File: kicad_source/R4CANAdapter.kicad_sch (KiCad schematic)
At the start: 32 parts, among them CN1 CONN_01X05, CN2 691322310004, CN3 GH_SM04B-GHS-TB, CN4 GH_SM04B-GHS-TB, CN5 SM04B-SRSS-TB, Q1 2N7002, Q2 2N7002, U1 MCP2551-I/SN, U2 24LC64

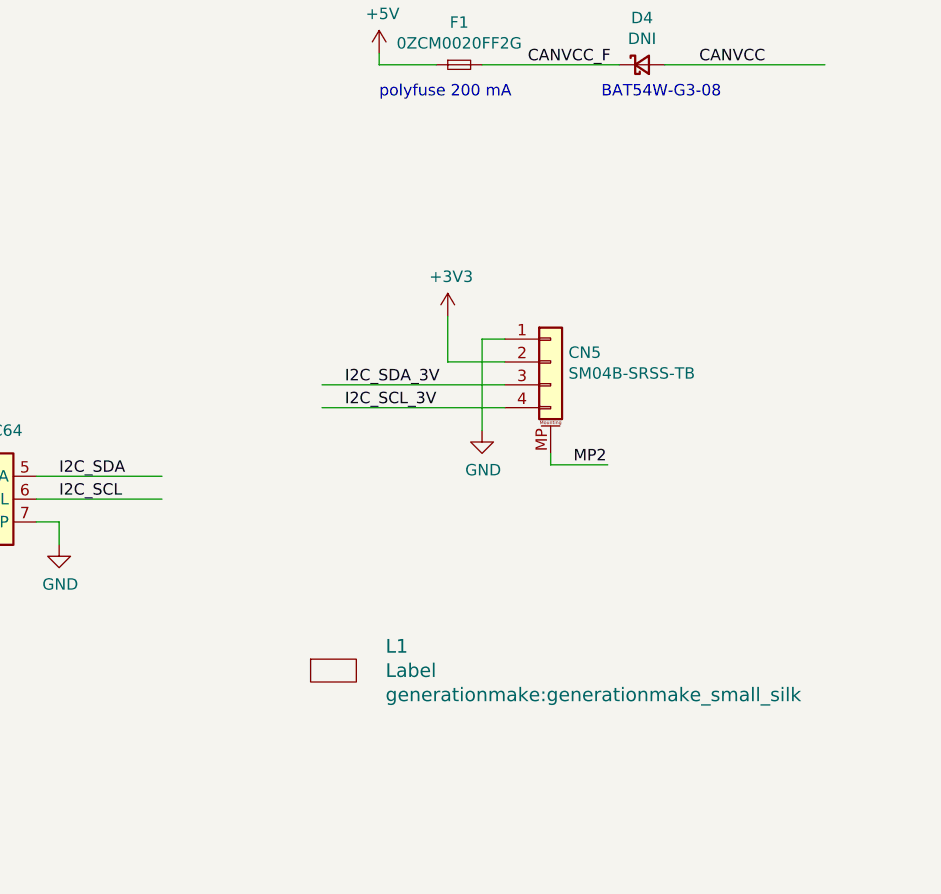
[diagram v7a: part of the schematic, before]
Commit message: added some labels, beautified layout, made DRC
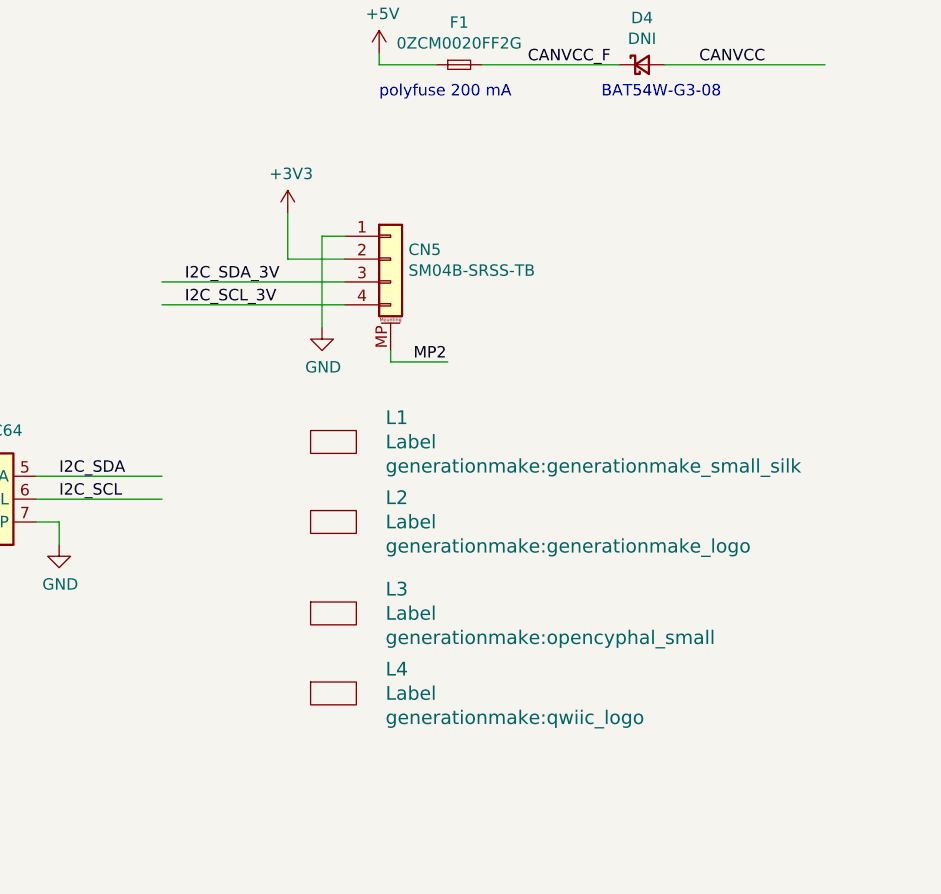
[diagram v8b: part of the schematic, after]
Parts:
- added L2: Label, generationmake:generationmake_logo, symbol generationmake:Label
- added L3: Label, generationmake:opencyphal_small, symbol generationmake:Label
- added L4: Label, generationmake:qwiic_logo, symbol generationmake:Label
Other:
- moved on the sheet: CN5, L1
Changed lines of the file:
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@@
     (stroke (width 0) (type default) (color 0 0 0 0))
   )
-  (wire (pts (xy 243.84 119.38) (xy 237.49 119.38))
+  (wire (pts (xy 226.06 107.95) (xy 219.71 107.95))
     (stroke (width 0) (type default) (color 0 0 0 0))
   )
@@
     (stroke (width 0) (type default) (color 0 0 0 0))
   )
-  (wire (pts (xy 248.92 130.81) (xy 248.92 129.54))
+  (wire (pts (xy 231.14 119.38) (xy 231.14 118.11))
     (stroke (width 0) (type default) (color 0 0 0 0))
   )
@@
     (stroke (width 0) (type default) (color 0 0 0 0))
   )
-  (wire (pts (xy 241.3 116.84) (xy 241.3 127))
+  (wire (pts (xy 223.52 105.41) (xy 223.52 115.57))
     (stroke (width 0) (type default) (color 0 0 0 0))
   )
@@
     (stroke (width 0) (type default) (color 0 0 0 0))
   )
-  (wire (pts (xy 237.49 119.38) (xy 237.49 114.3))
+  (wire (pts (xy 219.71 107.95) (xy 219.71 102.87))
     (stroke (width 0) (type default) (color 0 0 0 0))
   )
@@
     (stroke (width 0) (type default) (color 0 0 0 0))
   )
-  (wire (pts (xy 255.27 130.81) (xy 248.92 130.81))
-    (stroke (width 0) (type default) (color 0 0 0 0))
-  )
-  (wire (pts (xy 223.52 121.92) (xy 243.84 121.92))
+  (wire (pts (xy 237.49 119.38) (xy 231.14 119.38))
+    (stroke (width 0) (type default) (color 0 0 0 0))
+  )
+  (wire (pts (xy 205.74 110.49) (xy 226.06 110.49))
     (stroke (width 0) (type default) (color 0 0 0 0))
   )
@@
     (stroke (width 0) (type default) (color 0 0 0 0))
   )
-  (wire (pts (xy 243.84 116.84) (xy 241.3 116.84))
+  (wire (pts (xy 226.06 105.41) (xy 223.52 105.41))
     (stroke (width 0) (type default) (color 0 0 0 0))
   )
@@
     (stroke (width 0) (type default) (color 0 0 0 0))
   )
-  (wire (pts (xy 223.52 124.46) (xy 243.84 124.46))
+  (wire (pts (xy 205.74 113.03) (xy 226.06 113.03))
     (stroke (width 0) (type default) (color 0 0 0 0))
   )
@@
     (effects (font (size 1.27 1.27)) (justify left bottom))
   )
-  (label "I2C_SDA_3V" (at 226.06 121.92 0)
+  (label "I2C_SDA_3V" (at 208.28 110.49 0)
     (effects (font (size 1.27 1.27)) (justify left bottom))
   )
@@
     (effects (font (size 1.27 1.27)) (justify left bottom))
   )
-  (label "MP2" (at 251.46 130.81 0)
+  (label "MP2" (at 233.68 119.38 0)
     (effects (font (size 1.27 1.27)) (justify left bottom))
   )
@@
     (effects (font (size 1.27 1.27)) (justify left bottom))
   )
-  (label "I2C_SCL_3V" (at 226.06 124.46 0)
+  (label "I2C_SCL_3V" (at 208.28 113.03 0)
     (effects (font (size 1.27 1.27)) (justify left bottom))
   )
@@
     (pin "1")
   )
-  (symbol (lib_id "generationmake:Label") (at 224.79 153.67 0) (unit 1)
-    (in_bom yes) (on_board yes)
-    (property "Reference" "L1" (id 0) (at 230.5812 150.9776 0)
+  (symbol (lib_id "generationmake:Label") (at 224.79 128.27 0) (unit 1)
+    (in_bom yes) (on_board yes)
+    (property "Reference" "L1" (id 0) (at 230.5812 125.5776 0)
       (effects (font (size 1.524 1.524)) (justify left))
     )
-    (property "Value" "Label" (id 1) (at 230.5812 153.67 0)
+    (property "Value" "Label" (id 1) (at 230.5812 128.27 0)
       (effects (font (size 1.524 1.524)) (justify left))
     )
-    (property "Footprint" "generationmake:generationmake_small_silk" (id 2) (at 230.5812 156.3624 0)
+    (property "Footprint" "generationmake:generationmake_small_silk" (id 2) (at 230.5812 130.9624 0)
       (effects (font (size 1.524 1.524)) (justify left))
     )
-    (property "Datasheet" "" (id 3) (at 224.79 153.67 0)
+    (property "Datasheet" "" (id 3) (at 224.79 128.27 0)
       (effects (font (size 1.524 1.524)))
     )
@@
     (pin "2")
   )
+  (symbol (lib_id "generationmake:Label") (at 224.79 147.32 0) (unit 1)
+    (in_bom yes) (on_board yes)
+    (property "Reference" "L3" (id 0) (at 230.5812 144.6276 0)
+      (effects (font (size 1.524 1.524)) (justify left))
+    )
+    (property "Value" "Label" (id 1) (at 230.5812 147.32 0)
+      (effects (font (size 1.524 1.524)) (justify left))
+    )
+    (property "Footprint" "generationmake:opencyphal_small" (id 2) (at 230.5812 150.0124 0)
+      (effects (font (size 1.524 1.524)) (justify left))
+    )
+    (property "Datasheet" "" (id 3) (at 224.79 147.32 0)
+      (effects (font (size 1.524 1.524)))
+    )
+  )
   (symbol (lib_id "Device:R_Small") (at 124.46 109.22 0) (unit 1)
     (in_bom yes) (on_board yes)
@@
     (pin "8")
   )
-  (symbol (lib_id "power:+3V3") (at 237.49 114.3 0) (unit 1)
-    (in_bom yes) (on_board yes)
-    (property "Reference" "#PWR021" (id 0) (at 237.49 118.11 0)
-      (effects (font (size 1.27 1.27)) hide)
-    )
-    (property "Value" "+3V3" (id 1) (at 237.871 109.9058 0))
-    (property "Footprint" "" (id 2) (at 237.49 114.3 0))
-    (property "Datasheet" "" (id 3) (at 237.49 114.3 0))
+  (symbol (lib_id "power:+3V3") (at 219.71 102.87 0) (unit 1)
+    (in_bom yes) (on_board yes)
+    (property "Reference" "#PWR021" (id 0) (at 219.71 106.68 0)
+      (effects (font (size 1.27 1.27)) hide)
+    )
+    (property "Value" "+3V3" (id 1) (at 220.091 98.4758 0))
+    (property "Footprint" "" (id 2) (at 219.71 102.87 0))
+    (property "Datasheet" "" (id 3) (at 219.71 102.87 0))
     (pin "1")
   )
@@
     (pin "1")
   )
+  (symbol (lib_id "generationmake:Label") (at 224.79 137.16 0) (unit 1)
+    (in_bom yes) (on_board yes)
+    (property "Reference" "L2" (id 0) (at 230.5812 134.4676 0)
+      (effects (font (size 1.524 1.524)) (justify left))
+    )
+    (property "Value" "Label" (id 1) (at 230.5812 137.16 0)
+      (effects (font (size 1.524 1.524)) (justify left))
+    )
+    (property "Footprint" "generationmake:generationmake_logo" (id 2) (at 230.5812 139.8524 0)
+      (effects (font (size 1.524 1.524)) (justify left))
+    )
+    (property "Datasheet" "" (id 3) (at 224.79 137.16 0)
+      (effects (font (size 1.524 1.524)))
+    )
+  )
   (symbol (lib_id "Device:Q_NMOS_GSD") (at 135.89 149.86 270) (unit 1)
     (in_bom yes) (on_board yes) (fields_autoplaced)
@@
     (pin "3")
   )
+  (symbol (lib_id "generationmake:Label") (at 224.79 156.21 0) (unit 1)
+    (in_bom yes) (on_board yes)
+    (property "Reference" "L4" (id 0) (at 230.5812 153.5176 0)
+      (effects (font (size 1.524 1.524)) (justify left))
+    )
+    (property "Value" "Label" (id 1) (at 230.5812 156.21 0)
+      (effects (font (size 1.524 1.524)) (justify left))
+    )
+    (property "Footprint" "generationmake:qwiic_logo" (id 2) (at 230.5812 158.9024 0)
+      (effects (font (size 1.524 1.524)) (justify left))
+    )
+    (property "Datasheet" "" (id 3) (at 224.79 156.21 0)
+      (effects (font (size 1.524 1.524)))
+    )
+  )
   (symbol (lib_id "power:GND") (at 181.61 143.51 0) (unit 1)
     (in_bom yes) (on_board yes)
@@
     (pin "1")
   )
-  (symbol (lib_id "Connector_Generic_MountingPin:Conn_01x04_MountingPin") (at 248.92 119.38 0) (unit 1)
-    (in_bom yes) (on_board yes)
-    (property "Reference" "CN5" (id 0) (at 250.9012 118.3386 0)
-      (effects (font (size 1.27 1.27)) (justify left))
-    )
-    (property "Value" "SM04B-SRSS-TB" (id 1) (at 250.9012 120.65 0)
-      (effects (font (size 1.27 1.27)) (justify left))
-    )
-    (property "Footprint" "Connector_JST:JST_SH_SM04B-SRSS-TB_1x04-1MP_P1.00mm_Horizontal" (id 2) (at 248.92 119.38 0)
-      (effects (font (size 1.27 1.27)) hide)
-    )
-    (property "Datasheet" "~" (id 3) (at 248.92 119.38 0)
+  (symbol (lib_id "Connector_Generic_MountingPin:Conn_01x04_MountingPin") (at 231.14 107.95 0) (unit 1)
+    (in_bom yes) (on_board yes)
+    (property "Reference" "CN5" (id 0) (at 233.1212 106.9086 0)
+      (effects (font (size 1.27 1.27)) (justify left))
+    )
+    (property "Value" "SM04B-SRSS-TB" (id 1) (at 233.1212 109.22 0)
+      (effects (font (size 1.27 1.27)) (justify left))
+    )
+    (property "Footprint" "Connector_JST:JST_SH_SM04B-SRSS-TB_1x04-1MP_P1.00mm_Horizontal" (id 2) (at 231.14 107.95 0)
+      (effects (font (size 1.27 1.27)) hide)
+    )
+    (property "Datasheet" "~" (id 3) (at 231.14 107.95 0)
       (effects (font (size 1.27 1.27)) hide)
     )
@@
     (pin "1")
   )
-  (symbol (lib_id "power:GND") (at 241.3 127 0) (unit 1)
-    (in_bom yes) (on_board yes)
-    (property "Reference" "#PWR022" (id 0) (at 241.3 133.35 0)
-      (effects (font (size 1.27 1.27)) hide)
-    )
-    (property "Value" "GND" (id 1) (at 241.427 131.3942 0))
-    (property "Footprint" "" (id 2) (at 241.3 127 0))
-    (property "Datasheet" "" (id 3) (at 241.3 127 0))
+  (symbol (lib_id "power:GND") (at 223.52 115.57 0) (unit 1)
+    (in_bom yes) (on_board yes)
+    (property "Reference" "#PWR022" (id 0) (at 223.52 121.92 0)
+      (effects (font (size 1.27 1.27)) hide)
+    )
+    (property "Value" "GND" (id 1) (at 223.647 119.9642 0))
+    (property "Footprint" "" (id 2) (at 223.52 115.57 0))
+    (property "Datasheet" "" (id 3) (at 223.52 115.57 0))
     (pin "1")
   )
@@
       (reference "L1") (unit 1) (value "Label") (footprint "generationmake:generationmake_small_silk")
     )
+    (path "/7a91fef7-a080-42c6-8df6-1016ca71ad0f"
+      (reference "L2") (unit 1) (value "Label") (footprint "generationmake:generationmake_logo")
+    )
+    (path "/1e3b68c6-0bb6-44ac-816a-ba79d2b285da"
+      (reference "L3") (unit 1) (value "Label") (footprint "generationmake:opencyphal_small")
+    )
+    (path "/8c6a4361-bd1c-4684-980a-aa84f654dba7"
+      (reference "L4") (unit 1) (value "Label") (footprint "generationmake:qwiic_logo")
+    )
     (path "/f2f807cd-8b50-406d-8b1f-3440547c2c22"
